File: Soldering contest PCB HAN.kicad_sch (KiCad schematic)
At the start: 0 parts

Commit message: Schematic created
Basic circuit has been drawn
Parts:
- added C? (x2): C_Polarized, symbol Device:C_Polarized
- added D? (x2): LED, symbol Device:LED
- added J?: Screw_Terminal_01x02, symbol Connector:Screw_Terminal_01x02
- added Q? (x2): 2N3904, Package_TO_SOT_THT:TO-92_Inline, symbol Transistor_BJT:2N3904
- added R? (x4): R, symbol Device:R
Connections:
- new net: D?.1 (K), R?.2 (x2)
- new net: D?.2 (A), D?.2 (A), J?.1 (Pin_1), R?.1, R?.1
- new net: C?.1, Q?.3 (C), R?.1 (x2)
- new net: C?.2, Q?.2 (B), R?.2 (x2)
- new net GND: J?.2 (Pin_2), Q?.1 (E), Q?.1 (E)

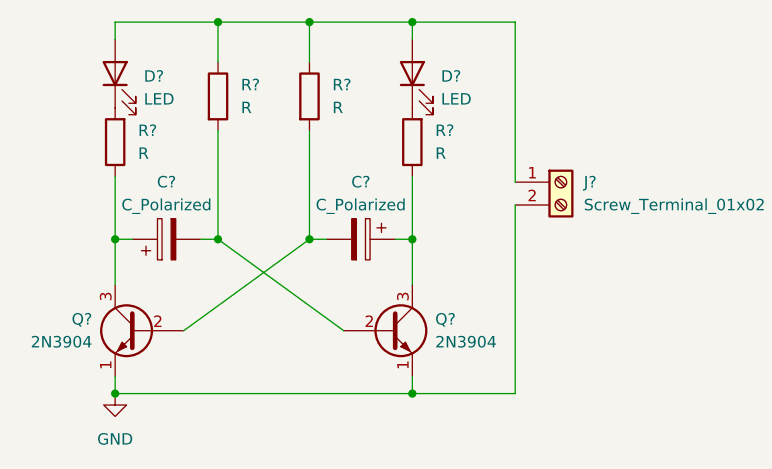
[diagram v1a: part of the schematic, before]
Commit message: added values and references to components
Some values may be tweaked later
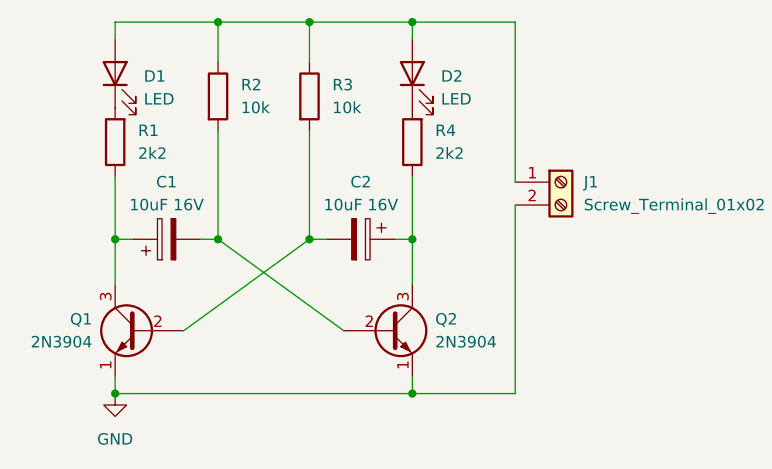
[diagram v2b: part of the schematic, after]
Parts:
- C1, C2: renamed from C?; value C_Polarized -> 10uF 16V
- R1, R4: renamed from R?; value R -> 2k2
- R2, R3: renamed from R?; value R -> 10k
- gave numbers to parts that had none: 5
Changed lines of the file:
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@@
   (symbol (lib_id "Device:LED") (at 147.32 80.645 90) (unit 1)
     (in_bom yes) (on_board yes) (fields_autoplaced)
-    (property "Reference" "D?" (id 0) (at 150.495 80.9624 90)
+    (property "Reference" "D2" (id 0) (at 150.495 80.9624 90)
       (effects (font (size 1.27 1.27)) (justify right))
     )
@@
   (symbol (lib_id "Device:C_Polarized") (at 141.605 99.06 270) (unit 1)
     (in_bom yes) (on_board yes)
-    (property "Reference" "C?" (id 0) (at 141.605 92.71 90))
-    (property "Value" "C_Polarized" (id 1) (at 141.605 95.25 90))
+    (property "Reference" "C2" (id 0) (at 141.605 92.71 90))
+    (property "Value" "10uF 16V" (id 1) (at 141.605 95.25 90))
     (property "Footprint" "" (id 2) (at 137.795 100.0252 0)
       (effects (font (size 1.27 1.27)) hide)
@@
   (symbol (lib_id "Transistor_BJT:2N3904") (at 144.78 109.22 0) (unit 1)
     (in_bom yes) (on_board yes) (fields_autoplaced)
-    (property "Reference" "Q?" (id 0) (at 149.86 107.9499 0)
+    (property "Reference" "Q2" (id 0) (at 149.86 107.9499 0)
       (effects (font (size 1.27 1.27)) (justify left))
     )
@@
   (symbol (lib_id "Connector:Screw_Terminal_01x02") (at 163.83 92.71 0) (unit 1)
     (in_bom yes) (on_board yes) (fields_autoplaced)
-    (property "Reference" "J?" (id 0) (at 166.37 92.7099 0)
+    (property "Reference" "J1" (id 0) (at 166.37 92.7099 0)
       (effects (font (size 1.27 1.27)) (justify left))
     )
@@
   (symbol (lib_id "Device:R") (at 147.32 88.265 180) (unit 1)
     (in_bom yes) (on_board yes) (fields_autoplaced)
-    (property "Reference" "R?" (id 0) (at 149.86 86.9949 0)
-      (effects (font (size 1.27 1.27)) (justify right))
-    )
-    (property "Value" "R" (id 1) (at 149.86 89.5349 0)
+    (property "Reference" "R4" (id 0) (at 149.86 86.9949 0)
+      (effects (font (size 1.27 1.27)) (justify right))
+    )
+    (property "Value" "2k2" (id 1) (at 149.86 89.5349 0)
       (effects (font (size 1.27 1.27)) (justify right))
     )
@@
   (symbol (lib_id "Device:C_Polarized") (at 120.015 99.06 90) (unit 1)
     (in_bom yes) (on_board yes)
-    (property "Reference" "C?" (id 0) (at 120.015 92.71 90))
-    (property "Value" "C_Polarized" (id 1) (at 120.015 95.25 90))
+    (property "Reference" "C1" (id 0) (at 120.015 92.71 90))
+    (property "Value" "10uF 16V" (id 1) (at 120.015 95.25 90))
     (property "Footprint" "" (id 2) (at 123.825 98.0948 0)
       (effects (font (size 1.27 1.27)) hide)
@@
   (symbol (lib_id "Device:R") (at 125.73 83.185 0) (unit 1)
     (in_bom yes) (on_board yes) (fields_autoplaced)
-    (property "Reference" "R?" (id 0) (at 128.27 81.9149 0)
-      (effects (font (size 1.27 1.27)) (justify left))
-    )
-    (property "Value" "R" (id 1) (at 128.27 84.4549 0)
+    (property "Reference" "R2" (id 0) (at 128.27 81.9149 0)
+      (effects (font (size 1.27 1.27)) (justify left))
+    )
+    (property "Value" "10k" (id 1) (at 128.27 84.4549 0)
       (effects (font (size 1.27 1.27)) (justify left))
     )
@@
   (symbol (lib_id "Device:R") (at 135.89 83.185 0) (unit 1)
     (in_bom yes) (on_board yes) (fields_autoplaced)
-    (property "Reference" "R?" (id 0) (at 138.43 81.9149 0)
-      (effects (font (size 1.27 1.27)) (justify left))
-    )
-    (property "Value" "R" (id 1) (at 138.43 84.4549 0)
+    (property "Reference" "R3" (id 0) (at 138.43 81.9149 0)
+      (effects (font (size 1.27 1.27)) (justify left))
+    )
+    (property "Value" "10k" (id 1) (at 138.43 84.4549 0)
       (effects (font (size 1.27 1.27)) (justify left))
     )
@@
   (symbol (lib_id "Transistor_BJT:2N3904") (at 116.84 109.22 0) (mirror y) (unit 1)
     (in_bom yes) (on_board yes) (fields_autoplaced)
-    (property "Reference" "Q?" (id 0) (at 111.76 107.9499 0)
+    (property "Reference" "Q1" (id 0) (at 111.76 107.9499 0)
       (effects (font (size 1.27 1.27)) (justify left))
     )
@@
   (symbol (lib_id "Device:LED") (at 114.3 80.645 90) (unit 1)
     (in_bom yes) (on_board yes) (fields_autoplaced)
-    (property "Reference" "D?" (id 0) (at 117.475 80.9624 90)
+    (property "Reference" "D1" (id 0) (at 117.475 80.9624 90)
       (effects (font (size 1.27 1.27)) (justify right))
     )
@@
   (symbol (lib_id "Device:R") (at 114.3 88.265 180) (unit 1)
     (in_bom yes) (on_board yes) (fields_autoplaced)
-    (property "Reference" "R?" (id 0) (at 116.84 86.9949 0)
-      (effects (font (size 1.27 1.27)) (justify right))
-    )
-    (property "Value" "R" (id 1) (at 116.84 89.5349 0)
+    (property "Reference" "R1" (id 0) (at 116.84 86.9949 0)
+      (effects (font (size 1.27 1.27)) (justify right))
+    )
+    (property "Value" "2k2" (id 1) (at 116.84 89.5349 0)
       (effects (font (size 1.27 1.27)) (justify right))
     )
@@
   (symbol (lib_id "power:GND") (at 114.3 116.205 0) (unit 1)
     (in_bom yes) (on_board yes) (fields_autoplaced)
-    (property "Reference" "#PWR?" (id 0) (at 114.3 122.555 0)
+    (property "Reference" "#PWR01" (id 0) (at 114.3 122.555 0)
       (effects (font (size 1.27 1.27)) hide)
     )
@@
   (symbol_instances
     (path "/ef9c6aea-c46c-4200-b0bd-f29d995fd9ba"
-      (reference "#PWR?") (unit 1) (value "GND") (footprint "")
+      (reference "#PWR01") (unit 1) (value "GND") (footprint "")
+    )
+    (path "/5c87c882-b6f1-48af-94eb-8b3a9c0bcf0b"
+      (reference "C1") (unit 1) (value "10uF 16V") (footprint "")
     )
     (path "/034eabb7-3f77-44d1-8a01-2675ee937952"
-      (reference "C?") (unit 1) (value "C_Polarized") (footprint "")
-    )
-    (path "/5c87c882-b6f1-48af-94eb-8b3a9c0bcf0b"
-      (reference "C?") (unit 1) (value "C_Polarized") (footprint "")
+      (reference "C2") (unit 1) (value "10uF 16V") (footprint "")
+    )
+    (path "/a7db6a88-2520-428c-8049-3d1f48bb4462"
+      (reference "D1") (unit 1) (value "LED") (footprint "")
     )
     (path "/007cf9ca-568a-495d-bdcf-3b4e025b88a0"
-      (reference "D?") (unit 1) (value "LED") (footprint "")
-    )
-    (path "/a7db6a88-2520-428c-8049-3d1f48bb4462"
-      (reference "D?") (unit 1) (value "LED") (footprint "")
+      (reference "D2") (unit 1) (value "LED") (footprint "")
     )
     (path "/0fe9d6fd-bdce-4016-adb7-83a4c7c35634"
-      (reference "J?") (unit 1) (value "Screw_Terminal_01x02") (footprint "")
+      (reference "J1") (unit 1) (value "Screw_Terminal_01x02") (footprint "")
+    )
+    (path "/6b424259-f8a0-4482-996c-adc9565aa863"
+      (reference "Q1") (unit 1) (value "2N3904") (footprint "Package_TO_SOT_THT:TO-92_Inline")
     )
     (path "/0fd58cd3-0637-4e39-b339-0859c358a065"
-      (reference "Q?") (unit 1) (value "2N3904") (footprint "Package_TO_SOT_THT:TO-92_Inline")
-    )
-    (path "/6b424259-f8a0-4482-996c-adc9565aa863"
-      (reference "Q?") (unit 1) (value "2N3904") (footprint "Package_TO_SOT_THT:TO-92_Inline")
+      (reference "Q2") (unit 1) (value "2N3904") (footprint "Package_TO_SOT_THT:TO-92_Inline")
+    )
+    (path "/d18fc897-0878-42f5-b8a2-449363703de6"
+      (reference "R1") (unit 1) (value "2k2") (footprint "")
+    )
+    (path "/5eba335f-f9b7-4f96-8244-9f11f5b02fc1"
+      (reference "R2") (unit 1) (value "10k") (footprint "")
+    )
+    (path "/5fd75fa8-c971-4180-8d4d-419bf5fd463a"
+      (reference "R3") (unit 1) (value "10k") (footprint "")
     )
     (path "/22a04216-54cb-44fe-9b76-e181b36e1a9f"
-      (reference "R?") (unit 1) (value "R") (footprint "")
-    )
-    (path "/5eba335f-f9b7-4f96-8244-9f11f5b02fc1"
-      (reference "R?") (unit 1) (value "R") (footprint "")
-    )
-    (path "/5fd75fa8-c971-4180-8d4d-419bf5fd463a"
-      (reference "R?") (unit 1) (value "R") (footprint "")
-    )
-    (path "/d18fc897-0878-42f5-b8a2-449363703de6"
-      (reference "R?") (unit 1) (value "R") (footprint "")
-    )
-  )
+      (reference "R4") (unit 1) (value "2k2") (footprint "")
+    )
+  )

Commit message: defined smd and tht sides of schematic
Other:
- note added: "SMD/SMT side of circuit"
- note added: "THT side of circuit"
- moved on the sheet: J1
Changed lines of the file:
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@@
   (junction (at 125.73 99.06) (diameter 0) (color 0 0 0 0)
   )
-  (wire (pts (xy 158.75 95.25) (xy 158.75 116.205))
+  (polyline (pts (xy 130.81 73.025) (xy 112.395 73.025))
+    (stroke (width 0) (type default) (color 0 0 0 0))
+  )
+  (polyline (pts (xy 130.81 114.3) (xy 130.81 73.025))
+    (stroke (width 0) (type default) (color 0 0 0 0))
+  )
+  (wire (pts (xy 158.75 95.885) (xy 158.75 116.205))
     (stroke (width 0) (type default) (color 0 0 0 0))
   )
@@
   )
   (wire (pts (xy 135.89 99.06) (xy 121.92 109.22))
+    (stroke (width 0) (type default) (color 0 0 0 0))
+  )
+  (polyline (pts (xy 130.81 73.025) (xy 130.81 77.47))
     (stroke (width 0) (type default) (color 0 0 0 0))
   )
@@
     (stroke (width 0) (type default) (color 0 0 0 0))
   )
-  (wire (pts (xy 158.75 74.93) (xy 158.75 92.71))
+  (polyline (pts (xy 112.395 114.3) (xy 165.735 114.3))
+    (stroke (width 0) (type default) (color 0 0 0 0))
+  )
+  (wire (pts (xy 158.75 74.93) (xy 158.75 93.345))
     (stroke (width 0) (type default) (color 0 0 0 0))
   )
   (wire (pts (xy 147.32 116.205) (xy 147.32 114.3))
+    (stroke (width 0) (type default) (color 0 0 0 0))
+  )
+  (polyline (pts (xy 112.395 73.025) (xy 112.395 114.3))
     (stroke (width 0) (type default) (color 0 0 0 0))
   )
@@
     (stroke (width 0) (type default) (color 0 0 0 0))
   )
+  (polyline (pts (xy 165.735 73.025) (xy 130.81 73.025))
+    (stroke (width 0) (type default) (color 0 0 0 0))
+  )
   (wire (pts (xy 114.3 99.06) (xy 114.3 104.14))
     (stroke (width 0) (type default) (color 0 0 0 0))
@@
     (stroke (width 0) (type default) (color 0 0 0 0))
   )
+  (polyline (pts (xy 165.735 114.3) (xy 165.735 73.025))
+    (stroke (width 0) (type default) (color 0 0 0 0))
+  )
   (wire (pts (xy 135.89 86.995) (xy 135.89 99.06))
     (stroke (width 0) (type default) (color 0 0 0 0))
+  )
+  (text "SMD/SMT side of circuit\n" (at 105.41 71.755 0)
+    (effects (font (size 1.27 1.27)) (justify left bottom))
+  )
+  (text "THT side of circuit\n" (at 137.795 71.755 0)
+    (effects (font (size 1.27 1.27)) (justify left bottom))
   )
   (symbol (lib_id "Device:LED") (at 147.32 80.645 90) (unit 1)
@@
     (pin "3")
   )
-  (symbol (lib_id "Connector:Screw_Terminal_01x02") (at 163.83 92.71 0) (unit 1)
+  (symbol (lib_id "Connector:Screw_Terminal_01x02") (at 163.83 93.345 0) (unit 1)
     (in_bom yes) (on_board yes) (fields_autoplaced)
-    (property "Reference" "J1" (id 0) (at 166.37 92.7099 0)
+    (property "Reference" "J1" (id 0) (at 166.37 93.3449 0)
       (effects (font (size 1.27 1.27)) (justify left))
     )
-    (property "Value" "Screw_Terminal_01x02" (id 1) (at 166.37 95.2499 0)
+    (property "Value" "Screw_Terminal_01x02" (id 1) (at 166.37 95.8849 0)
       (effects (font (size 1.27 1.27)) (justify left))
     )
-    (property "Footprint" "" (id 2) (at 163.83 92.71 0)
+    (property "Footprint" "" (id 2) (at 163.83 93.345 0)
       (effects (font (size 1.27 1.27)) hide)
     )
-    (property "Datasheet" "~" (id 3) (at 163.83 92.71 0)
+    (property "Datasheet" "~" (id 3) (at 163.83 93.345 0)
       (effects (font (size 1.27 1.27)) hide)
     )

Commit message: assigned footprints
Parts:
- C1: footprint (none) -> Capacitor_SMD:C_1206_3216Metric_Pad1.33x1.80mm_HandSolder
- C2: footprint (none) -> Capacitor_THT:CP_Radial_D4.0mm_P2.00mm
- D1: footprint (none) -> LED_SMD:LED_0805_2012Metric_Pad1.15x1.40mm_HandSolder
- D2: footprint (none) -> LED_THT:LED_D5.0mm_Clear
- J1: footprint (none) -> TerminalBlock:TerminalBlock_bornier-2_P5.08mm
- R1: footprint (none) -> Resistor_SMD:R_01005_0402Metric_Pad0.57x0.30mm_HandSolder
- R2: footprint (none) -> Resistor_SMD:R_0805_2012Metric_Pad1.20x1.40mm_HandSolder
- R3: footprint (none) -> Resistor_THT:R_Axial_DIN0207_L6.3mm_D2.5mm_P5.08mm_Vertical
- R4: footprint (none) -> Resistor_THT:R_Axial_DIN0207_L6.3mm_D2.5mm_P7.62mm_Horizontal
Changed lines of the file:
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@@
       (effects (font (size 1.27 1.27)) (justify right))
     )
-    (property "Footprint" "" (id 2) (at 147.32 80.645 0)
+    (property "Footprint" "LED_THT:LED_D5.0mm_Clear" (id 2) (at 147.32 80.645 0)
       (effects (font (size 1.27 1.27)) hide)
     )
@@
     (property "Reference" "C2" (id 0) (at 141.605 92.71 90))
     (property "Value" "10uF 16V" (id 1) (at 141.605 95.25 90))
-    (property "Footprint" "" (id 2) (at 137.795 100.0252 0)
+    (property "Footprint" "Capacitor_THT:CP_Radial_D4.0mm_P2.00mm" (id 2) (at 137.795 100.0252 0)
       (effects (font (size 1.27 1.27)) hide)
     )
@@
       (effects (font (size 1.27 1.27)) (justify left))
     )
-    (property "Footprint" "" (id 2) (at 163.83 93.345 0)
+    (property "Footprint" "TerminalBlock:TerminalBlock_bornier-2_P5.08mm" (id 2) (at 163.83 93.345 0)
       (effects (font (size 1.27 1.27)) hide)
     )
@@
       (effects (font (size 1.27 1.27)) (justify right))
     )
-    (property "Footprint" "" (id 2) (at 149.098 88.265 90)
+    (property "Footprint" "Resistor_THT:R_Axial_DIN0207_L6.3mm_D2.5mm_P7.62mm_Horizontal" (id 2) (at 149.098 88.265 90)
       (effects (font (size 1.27 1.27)) hide)
     )
@@
     (property "Reference" "C1" (id 0) (at 120.015 92.71 90))
     (property "Value" "10uF 16V" (id 1) (at 120.015 95.25 90))
-    (property "Footprint" "" (id 2) (at 123.825 98.0948 0)
+    (property "Footprint" "Capacitor_SMD:C_1206_3216Metric_Pad1.33x1.80mm_HandSolder" (id 2) (at 123.825 98.0948 0)
       (effects (font (size 1.27 1.27)) hide)
     )
@@
       (effects (font (size 1.27 1.27)) (justify left))
     )
-    (property "Footprint" "" (id 2) (at 123.952 83.185 90)
+    (property "Footprint" "Resistor_SMD:R_0805_2012Metric_Pad1.20x1.40mm_HandSolder" (id 2) (at 123.952 83.185 90)
       (effects (font (size 1.27 1.27)) hide)
     )
@@
       (effects (font (size 1.27 1.27)) (justify left))
     )
-    (property "Footprint" "" (id 2) (at 134.112 83.185 90)
+    (property "Footprint" "Resistor_THT:R_Axial_DIN0207_L6.3mm_D2.5mm_P5.08mm_Vertical" (id 2) (at 134.112 83.185 90)
       (effects (font (size 1.27 1.27)) hide)
     )
@@
       (effects (font (size 1.27 1.27)) (justify right))
     )
-    (property "Footprint" "" (id 2) (at 114.3 80.645 0)
+    (property "Footprint" "LED_SMD:LED_0805_2012Metric_Pad1.15x1.40mm_HandSolder" (id 2) (at 114.3 80.645 0)
       (effects (font (size 1.27 1.27)) hide)
     )
@@
       (effects (font (size 1.27 1.27)) (justify right))
     )
-    (property "Footprint" "" (id 2) (at 116.078 88.265 90)
+    (property "Footprint" "Resistor_SMD:R_01005_0402Metric_Pad0.57x0.30mm_HandSolder" (id 2) (at 116.078 88.265 90)
       (effects (font (size 1.27 1.27)) hide)
     )
@@
     )
     (path "/5c87c882-b6f1-48af-94eb-8b3a9c0bcf0b"
-      (reference "C1") (unit 1) (value "10uF 16V") (footprint "")
+      (reference "C1") (unit 1) (value "10uF 16V") (footprint "Capacitor_SMD:C_1206_3216Metric_Pad1.33x1.80mm_HandSolder")
     )
     (path "/034eabb7-3f77-44d1-8a01-2675ee937952"
-      (reference "C2") (unit 1) (value "10uF 16V") (footprint "")
+      (reference "C2") (unit 1) (value "10uF 16V") (footprint "Capacitor_THT:CP_Radial_D4.0mm_P2.00mm")
     )
     (path "/a7db6a88-2520-428c-8049-3d1f48bb4462"
-      (reference "D1") (unit 1) (value "LED") (footprint "")
+      (reference "D1") (unit 1) (value "LED") (footprint "LED_SMD:LED_0805_2012Metric_Pad1.15x1.40mm_HandSolder")
     )
     (path "/007cf9ca-568a-495d-bdcf-3b4e025b88a0"
-      (reference "D2") (unit 1) (value "LED") (footprint "")
+      (reference "D2") (unit 1) (value "LED") (footprint "LED_THT:LED_D5.0mm_Clear")
     )
     (path "/0fe9d6fd-bdce-4016-adb7-83a4c7c35634"
-      (reference "J1") (unit 1) (value "Screw_Terminal_01x02") (footprint "")
+      (reference "J1") (unit 1) (value "Screw_Terminal_01x02") (footprint "TerminalBlock:TerminalBlock_bornier-2_P5.08mm")
     )
     (path "/6b424259-f8a0-4482-996c-adc9565aa863"
@@
     )
     (path "/d18fc897-0878-42f5-b8a2-449363703de6"
-      (reference "R1") (unit 1) (value "2k2") (footprint "")
+      (reference "R1") (unit 1) (value "2k2") (footprint "Resistor_SMD:R_01005_0402Metric_Pad0.57x0.30mm_HandSolder")
     )
     (path "/5eba335f-f9b7-4f96-8244-9f11f5b02fc1"
-      (reference "R2") (unit 1) (value "10k") (footprint "")
+      (reference "R2") (unit 1) (value "10k") (footprint "Resistor_SMD:R_0805_2012Metric_Pad1.20x1.40mm_HandSolder")
     )
     (path "/5fd75fa8-c971-4180-8d4d-419bf5fd463a"
-      (reference "R3") (unit 1) (value "10k") (footprint "")
+      (reference "R3") (unit 1) (value "10k") (footprint "Resistor_THT:R_Axial_DIN0207_L6.3mm_D2.5mm_P5.08mm_Vertical")
     )
     (path "/22a04216-54cb-44fe-9b76-e181b36e1a9f"
-      (reference "R4") (unit 1) (value "2k2") (footprint "")
-    )
-  )
+      (reference "R4") (unit 1) (value "2k2") (footprint "Resistor_THT:R_Axial_DIN0207_L6.3mm_D2.5mm_P7.62mm_Horizontal")
+    )
+  )
